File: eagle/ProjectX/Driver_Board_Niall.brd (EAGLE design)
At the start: 100 x 100 mm, 185 parts, among them IC2 NCV78M05BDTRKG, J1 694102303002, U1 TC4427AEOA, U10 TC4427AEOA, U11 TC4427AEOA, U12 TC4427AEOA, U1200 CD74HC4067SM96, U13 TC4427AEOA, U14 TC4427AEOA, U15 TC4427AEOA, U16 TC4427AEOA, U17 TC4427AEOA, U18 TC4427AEOA, U19 TC4427AEOA, U2 TC4427AEOA, U20 TC4427AEOA, U200 ADA4091-2ARZ-RL, U21 TC4427AEOA, U22 TC4427AEOA, U23 TC4427AEOA, U24 TC4427AEOA, U25 TC4427AEOA, U26 TC4427AEOA, U27 TC4427AEOA, U28 TC4427AEOA, U29 TC4427AEOA, U3 TC4427AEOA, U30 TC4427AEOA, U31 TC4427AEOA, U32 TC4427AEOA, U33 TC4427AEOA, U34 TC4427AEOA, U35 TC4427AEOA, U36 TC4427AEOA, U37 TC4427AEOA, U38 TC4427AEOA, U39 TC4427AEOA, U4 TC4427AEOA, U40 TC4427AEOA, U41 TC4427AEOA, U42 TC4427AEOA, U43 TC4427AEOA, U44 TC4427AEOA, U45 TC4427AEOA, U46 TC4427AEOA, U47 TC4427AEOA, U48 TC4427AEOA, U49 TC4427AEOA, U5 TC4427AEOA, U50 TC4427AEOA, U6 TC4427AEOA, U7 TC4427AEOA, U8 TC4427AEOA, U9 TC4427AEOA

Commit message: Niall Boards new layout that should slot together
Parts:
- removed TP1, TP2: TPSTP10SQ, testpad:TP10SQ
- removed TRANSDUCERS_1, TRANSDUCERS_2, TRANSDUCERS_3, TRANSDUCERS_4: 40_PIN_SMD, Parts:40_PIN_SMD
- removed TRANSDUCERS_5: (no value), pinhead:2X20
- added 1, 2, 3, 4: PHB_1MM27_2X25_SNS, _hhn_con_pinhead_box_1mm27:PHB_1MM27_2X25_SNS
- moved LED_8 129.3 mm to (-12.9, 110.2)
- moved LED_9 128.5 mm to (-11.9, 95.4)
- moved LED_7 128.1 mm to (-12.9, 123.1)
- moved LED_10 126.9 mm to (-9.51, 81.2)
- moved 5V-REG 63.9 mm to (2.09, 64.4), turned to 270 degrees
- moved U40 56.3 mm to (72.4, 61.9), turned to 90 degrees
- moved DATA_2 55.1 mm to (-24.1, 61.7)
- moved C40 54.0 mm to (69.0, 61.9), turned to 90 degrees
- moved C12 50.5 mm to (38.5, 54.0), turned to 180 degrees
- moved U38 49.3 mm to (64.2, 61.7), turned to 90 degrees
- moved LED_6 49.0 mm to (-8.36, 72.7)
- moved C38 48.0 mm to (60.7, 61.7), turned to 90 degrees
- moved U12 47.5 mm to (38.5, 50.3), turned to 180 degrees
- moved U20 47.0 mm to (38.5, 7.11), turned to 180 degrees
- moved C29 44.9 mm to (38.5, 46.7), turned to 180 degrees
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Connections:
- removed net N$23: DIP2.8, TP1.TP
- removed net N$24: DIP2.9, TP2.TP
- removed net N$25: DATA_2.9, DIP2.190
- removed net N$26: DATA_2.7, DIP2.193
- removed net N$27: DATA_2.5, DIP2.197
- removed net N$28: DATA_2.1, DIP2.203
- removed net N$29: DATA_2.3, DIP2.200
- net +5V: no longer DATA_1.1
- net 1: now also DIP2.75; no longer DIP2.77
- net 10: now also DIP2.47; no longer DIP2.41
- net 100: now also DIP2.137; no longer DIP2.162
- net 11: now also DIP2.48; no longer DIP2.39
- net 12: now also DIP2.50; no longer DIP2.35
- net 13: now also DIP2.40; no longer DIP2.33
- net 14: now also DIP2.36; no longer DIP2.30
- net 15: now also DIP2.60; no longer DIP2.28
- net 16: now also DIP2.62; no longer DIP2.24
- net 17: now also DIP2.29; no longer DIP2.22
- net 18: now also DIP2.23; no longer DIP2.18
- net 19: now also DIP2.64; no longer DIP2.15
- net 2: now also DIP2.77; no longer DIP2.75
- net 20: now also DIP2.69; no longer DIP2.11
- net 21: now also DIP2.19; no longer DIP2.82
- net 22: now also DIP2.25; no longer DIP2.76
- net 23: now also DIP2.192; no longer DIP2.74
- net 24: now also DIP2.196; no longer DIP2.65
- net 25: now also DIP2.102; no longer DIP2.63
- net 26: now also DIP2.109; no longer DIP2.61
- net 27: now also DIP2.31; no longer DIP2.55
- net 28: now also DIP2.34; no longer DIP2.49
- net 29: now also DIP2.133; no longer DIP2.47
- net 3: now also DIP2.35; no longer DIP2.69
- net 30: now also DIP2.138; no longer DIP2.42
- net 31: now also DIP2.42; no longer DIP2.40
- net 32: now also DIP2.49; no longer DIP2.36
- net 33: now also DIP2.145; no longer DIP2.34
- net 34: now also DIP2.151; no longer DIP2.31
- net 35: now also DIP2.61; no longer DIP2.29
- net 36: now also DIP2.65; no longer DIP2.25
- net 37: now also DIP2.189; no longer DIP2.23
- net 38: now also DIP2.186; no longer DIP2.19
- net 39: now also DIP2.76; no longer DIP2.16
- net 4: now also DIP2.39; no longer DIP2.64
- net 40: now also DIP2.82; no longer DIP2.12
- net 41: now also DIP2.16; no longer DIP2.165
- net 42: now also DIP2.9; no longer DIP2.168
- net 43: now also DIP2.202; no longer DIP2.178
- net 44: now also DIP2.199; no longer DIP2.181
- net 45: now also DIP2.126; no longer DIP2.138
- net 46: now also DIP2.128; no longer DIP2.135
- net 47: now also DIP2.164; no longer DIP2.133
- net 48: now also DIP2.167; no longer DIP2.129
- net 49: now also DIP2.147; no longer DIP2.127
- net 5: now also DIP2.74; no longer DIP2.62
- net 50: now also DIP2.140; no longer DIP2.123
- net 51: now also DIP2.135; no longer DIP2.120
- net 52: now also DIP2.129; no longer DIP2.116
- net 53: now also DIP2.116; no longer DIP2.107
- net 54: now also DIP2.123; no longer DIP2.102
- net 55: now also DIP2.127; no longer DIP2.113
- net 56: now also DIP2.120; no longer DIP2.109
- net 57: now also DIP2.205; no longer DIP2.99
- net 58: now also DIP2.12; no longer DIP2.97
- net 59: now also DIP2.90; no longer DIP2.94
- net 6: now also DIP2.63; no longer DIP2.60
- net 60: now also DIP2.97; no longer DIP2.90
- net 61: now also DIP2.99; no longer DIP2.152
- net 62: now also DIP2.94; no longer DIP2.150
- net 63: now also DIP2.113; no longer DIP2.139
- net 64: now also DIP2.107; no longer DIP2.137
- net 65: now also DIP2.93; no longer DIP2.146
- net 66: now also DIP2.96; no longer DIP2.144
- net 67: now also DIP2.98; no longer DIP2.128
- net 68: now also DIP2.100; no longer DIP2.126
- net 69: now also DIP2.106; no longer DIP2.134
- net 7: now also DIP2.41; no longer DIP2.50
- net 70: now also DIP2.108; no longer DIP2.132
- net 71: now also DIP2.112; no longer DIP2.115
- net 72: now also DIP2.115; no longer DIP2.112
- net 73: now also DIP2.119; no longer DIP2.122
- net 74: now also DIP2.122; no longer DIP2.119
- net 75: now also DIP2.178; no longer DIP2.108
- net 76: now also DIP2.180; no longer DIP2.106
- net 77: now also DIP2.162; no longer DIP2.100
- net 78: now also DIP2.165; no longer DIP2.98
- net 79: now also DIP2.185; no longer DIP2.96
- net 8: now also DIP2.45; no longer DIP2.48
- net 80: now also DIP2.187; no longer DIP2.93
- net 81: now also DIP2.153; no longer DIP2.186
- net 82: now also DIP2.160; no longer DIP2.180
- net 83: now also DIP2.190; no longer DIP2.185
- net 84: now also DIP2.193; no longer DIP2.189
- net 85: now also DIP2.172; no longer DIP2.171
- net 86: now also DIP2.168; no longer DIP2.167
- net 87: now also DIP2.177; no longer DIP2.187
- net 88: now also DIP2.171; no longer DIP2.172
- net 89: now also DIP2.163; no longer DIP2.145
- net 9: now also DIP2.55; no longer DIP2.45
- net 90: now also DIP2.161; no longer DIP2.147
- net 92: now also DIP2.181; no longer DIP2.177
- net 93: now also DIP2.146; no longer DIP2.151
- net 94: now also DIP2.144; no longer DIP2.153
- net 95: now also DIP2.152; no longer DIP2.163
- net 96: now also DIP2.150; no longer DIP2.161
- net 97: now also DIP2.134; no longer DIP2.160
- net 98: now also DIP2.132; no longer DIP2.140
- net 99: now also DIP2.139; no longer DIP2.164
- net FROM_TRANS_100: now also 1.2; no longer TRANSDUCERS_5.1
- net FROM_TRANS_85: now also 1.50; no longer TRANSDUCERS_5.31
- net FROM_TRANS_86: now also 1.48; no longer TRANSDUCERS_5.29
- net FROM_TRANS_87: now also 1.46; no longer TRANSDUCERS_5.27
- net FROM_TRANS_88: now also 1.44; no longer TRANSDUCERS_5.25
- net FROM_TRANS_89: now also 1.42; no longer TRANSDUCERS_5.23
- net FROM_TRANS_90: now also 1.40; no longer TRANSDUCERS_5.21
- net FROM_TRANS_91: now also 1.38; no longer TRANSDUCERS_5.19
- net FROM_TRANS_92: now also 1.36; no longer TRANSDUCERS_5.17
- net FROM_TRANS_93: now also 1.16; no longer TRANSDUCERS_5.15
- net FROM_TRANS_94: now also 1.14; no longer TRANSDUCERS_5.13
- net FROM_TRANS_95: now also 1.12; no longer TRANSDUCERS_5.11
- net FROM_TRANS_96: now also 1.10; no longer TRANSDUCERS_5.9
- net FROM_TRANS_97: now also 1.8; no longer TRANSDUCERS_5.7
- net FROM_TRANS_98: now also 1.6; no longer TRANSDUCERS_5.5
- net FROM_TRANS_99: now also 1.4; no longer TRANSDUCERS_5.3
- net GND: now also 1.18, 1.20, 1.22, 1.24, 1.26, 1.28, 1.30, 1.32, 1.34, 2.10, 2.11, 2.14, 2.15, 2.18, 2.19, 2.2, 2.22, 2.23, 2.26, 2.27, 2.3, 2.30, 2.31, 2.34, 2.35, 2.38, 2.39, 2.42, 2.43, 2.46, 2.47, 2.50, 2.6, 2.7, 3.10, 3.11, 3.14, 3.15, 3.18, 3.19, 3.2, 3.22, 3.23, 3.26, 3.27, 3.3, 3.30, 3.31, 3.34, 3.35, 3.38, 3.39, 3.42, 3.43, 3.46, 3.47, 3.50, 3.6, 3.7, 4.10, 4.11, 4.14, 4.15, 4.18, 4.19, 4.2, 4.22, 4.23, 4.26, 4.27, 4.3, 4.30, 4.31, 4.34, 4.35, 4.38, 4.39, 4.42, 4.43, 4.46, 4.47, 4.50, 4.6, 4.7; no longer DATA_1.2, DATA_2.2, TRANSDUCERS_1.1, TRANSDUCERS_1.11, TRANSDUCERS_1.13, TRANSDUCERS_1.15, TRANSDUCERS_1.17, TRANSDUCERS_1.19, TRANSDUCERS_1.21, TRANSDUCERS_1.23, TRANSDUCERS_1.25, TRANSDUCERS_1.27, TRANSDUCERS_1.29, TRANSDUCERS_1.3, TRANSDUCERS_1.31, TRANSDUCERS_1.33, TRANSDUCERS_1.35, TRANSDUCERS_1.37, TRANSDUCERS_1.39, TRANSDUCERS_1.5, TRANSDUCERS_1.7, TRANSDUCERS_1.9, TRANSDUCERS_2.1, TRANSDUCERS_2.11, TRANSDUCERS_2.13, TRANSDUCERS_2.15, TRANSDUCERS_2.17, TRANSDUCERS_2.19, TRANSDUCERS_2.21, TRANSDUCERS_2.23, TRANSDUCERS_2.25, TRANSDUCERS_2.27, TRANSDUCERS_2.29, TRANSDUCERS_2.3, TRANSDUCERS_2.31, TRANSDUCERS_2.33, TRANSDUCERS_2.35, TRANSDUCERS_2.37, TRANSDUCERS_2.39, TRANSDUCERS_2.5, TRANSDUCERS_2.7, TRANSDUCERS_2.9, TRANSDUCERS_3.1, TRANSDUCERS_3.11, TRANSDUCERS_3.13, TRANSDUCERS_3.15, TRANSDUCERS_3.17, TRANSDUCERS_3.19, TRANSDUCERS_3.21, TRANSDUCERS_3.23, TRANSDUCERS_3.25, TRANSDUCERS_3.27, TRANSDUCERS_3.29, TRANSDUCERS_3.3, TRANSDUCERS_3.31, TRANSDUCERS_3.33, TRANSDUCERS_3.35, TRANSDUCERS_3.37, TRANSDUCERS_3.39, TRANSDUCERS_3.5, TRANSDUCERS_3.7, TRANSDUCERS_3.9, TRANSDUCERS_4.1, TRANSDUCERS_4.11, TRANSDUCERS_4.13, TRANSDUCERS_4.15, TRANSDUCERS_4.17, TRANSDUCERS_4.19, TRANSDUCERS_4.21, TRANSDUCERS_4.23, TRANSDUCERS_4.25, TRANSDUCERS_4.27, TRANSDUCERS_4.29, TRANSDUCERS_4.3, TRANSDUCERS_4.31, TRANSDUCERS_4.33, TRANSDUCERS_4.35, TRANSDUCERS_4.37, TRANSDUCERS_4.39, TRANSDUCERS_4.5, TRANSDUCERS_4.7, TRANSDUCERS_4.9, TRANSDUCERS_5.33, TRANSDUCERS_5.35, TRANSDUCERS_5.37, TRANSDUCERS_5.39
- net TEENSY_DATA_0: no longer DATA_1.7
- net TEENSY_DATA_1: no longer DATA_1.9
- net TEENSY_DATA_10: no longer DATA_2.10
- net TEENSY_DATA_11: no longer DATA_1.5
- net TEENSY_DATA_12: no longer DATA_1.3
- net TEENSY_DATA_2: no longer DATA_1.4
- net TEENSY_DATA_3: no longer DATA_1.6
- net TEENSY_DATA_31: no longer DIP2.3
- net TEENSY_DATA_32: no longer DIP2.5
- net TEENSY_DATA_33: no longer DIP2.2
- net TEENSY_DATA_34: no longer DIP2.4
- net TEENSY_DATA_4: no longer DATA_1.8
- net TEENSY_DATA_5: no longer DATA_1.10
- net TEENSY_DATA_7: no longer DATA_2.4
- net TEENSY_DATA_8: no longer DATA_2.6
- net TEENSY_DATA_9: no longer DATA_2.8
- net TO_TRAN_1: now also 4.9; no longer TRANSDUCERS_1.2
- net TO_TRAN_10: now also 4.16; no longer TRANSDUCERS_1.20
- net TO_TRAN_100: now also 1.1; no longer TRANSDUCERS_5.2
- net TO_TRAN_11: now also 4.33; no longer TRANSDUCERS_1.22
- net TO_TRAN_12: now also 4.29; no longer TRANSDUCERS_1.24
- net TO_TRAN_13: now also 4.20; no longer TRANSDUCERS_1.26
- net TO_TRAN_14: now also 4.24; no longer TRANSDUCERS_1.28
- net TO_TRAN_15: now also 4.25; no longer TRANSDUCERS_1.30
- net TO_TRAN_16: now also 4.21; no longer TRANSDUCERS_1.32
- net TO_TRAN_17: now also 4.28; no longer TRANSDUCERS_1.34
- net TO_TRAN_18: now also 4.32; no longer TRANSDUCERS_1.36
- net TO_TRAN_19: now also 4.17; no longer TRANSDUCERS_1.38
- net TO_TRAN_2: now also 4.5; no longer TRANSDUCERS_1.4
- net TO_TRAN_20: now also 4.13; no longer TRANSDUCERS_1.40
- net TO_TRAN_21: now also 3.33; no longer TRANSDUCERS_2.2
- net TO_TRAN_22: now also 3.29; no longer TRANSDUCERS_2.4
- net TO_TRAN_23: now also 3.49; no longer TRANSDUCERS_2.6
- net TO_TRAN_24: now also 3.45; no longer TRANSDUCERS_2.8
- net TO_TRAN_25: now also 3.12; no longer TRANSDUCERS_2.10
- net TO_TRAN_26: now also 3.16; no longer TRANSDUCERS_2.12
- net TO_TRAN_27: now also 3.25; no longer TRANSDUCERS_2.14
- net TO_TRAN_28: now also 3.21; no longer TRANSDUCERS_2.16
- net TO_TRAN_29: now also 3.28; no longer TRANSDUCERS_2.18
- net TO_TRAN_3: now also 4.49; no longer TRANSDUCERS_1.6
- net TO_TRAN_30: now also 3.32; no longer TRANSDUCERS_2.20
- net TO_TRAN_31: now also 3.17; no longer TRANSDUCERS_2.22
- net TO_TRAN_32: now also 3.13; no longer TRANSDUCERS_2.24
- net TO_TRAN_33: now also 3.36; no longer TRANSDUCERS_2.26
- net TO_TRAN_34: now also 3.40; no longer TRANSDUCERS_2.28
- net TO_TRAN_35: now also 3.9; no longer TRANSDUCERS_2.30
- net TO_TRAN_36: now also 3.5; no longer TRANSDUCERS_2.32
- net TO_TRAN_37: now also 3.44; no longer TRANSDUCERS_2.34
- net TO_TRAN_38: now also 3.48; no longer TRANSDUCERS_2.36
- net TO_TRAN_39: now also 3.1; no longer TRANSDUCERS_2.38
- net TO_TRAN_4: now also 4.45; no longer TRANSDUCERS_1.8
- net TO_TRAN_40: now also 4.1; no longer TRANSDUCERS_2.40
- net TO_TRAN_41: now also 4.36; no longer TRANSDUCERS_3.2
- net TO_TRAN_42: now also 4.40; no longer TRANSDUCERS_3.4
- net TO_TRAN_43: now also 4.44; no longer TRANSDUCERS_3.6
- net TO_TRAN_44: now also 4.48; no longer TRANSDUCERS_3.8
- net TO_TRAN_45: now also 2.44; no longer TRANSDUCERS_3.10
- net TO_TRAN_46: now also 2.48; no longer TRANSDUCERS_3.12
- net TO_TRAN_47: now also 2.45; no longer TRANSDUCERS_3.14
- net TO_TRAN_48: now also 2.41; no longer TRANSDUCERS_3.16
- net TO_TRAN_49: now also 2.37; no longer TRANSDUCERS_3.18
- net TO_TRAN_5: now also 4.4; no longer TRANSDUCERS_1.10
- net TO_TRAN_50: now also 2.33; no longer TRANSDUCERS_3.20
- net TO_TRAN_51: now also 2.29; no longer TRANSDUCERS_3.22
- net TO_TRAN_52: now also 2.25; no longer TRANSDUCERS_3.24
- net TO_TRAN_53: now also 3.20; no longer TRANSDUCERS_3.26
- net TO_TRAN_54: now also 3.24; no longer TRANSDUCERS_3.28
- net TO_TRAN_55: now also 2.21; no longer TRANSDUCERS_3.30
- net TO_TRAN_56: now also 2.17; no longer TRANSDUCERS_3.32
- net TO_TRAN_57: now also 3.41; no longer TRANSDUCERS_3.34
- net TO_TRAN_58: now also 3.37; no longer TRANSDUCERS_3.36
- net TO_TRAN_59: now also 3.4; no longer TRANSDUCERS_3.38
- net TO_TRAN_6: now also 4.8; no longer TRANSDUCERS_1.12
- net TO_TRAN_60: now also 3.8; no longer TRANSDUCERS_3.40
- net TO_TRAN_61: now also 2.5; no longer TRANSDUCERS_4.2
- net TO_TRAN_62: now also 2.1; no longer TRANSDUCERS_4.4
- net TO_TRAN_63: now also 2.13; no longer TRANSDUCERS_4.6
- net TO_TRAN_64: now also 2.9; no longer TRANSDUCERS_4.8
- net TO_TRAN_65: now also 2.4; no longer TRANSDUCERS_4.10
- net TO_TRAN_66: now also 2.8; no longer TRANSDUCERS_4.12
- net TO_TRAN_67: now also 2.12; no longer TRANSDUCERS_4.14
- net TO_TRAN_68: now also 2.16; no longer TRANSDUCERS_4.16
- net TO_TRAN_69: now also 2.20; no longer TRANSDUCERS_4.18
- net TO_TRAN_7: now also 4.41; no longer TRANSDUCERS_1.14
- net TO_TRAN_70: now also 2.24; no longer TRANSDUCERS_4.20
- net TO_TRAN_71: now also 2.28; no longer TRANSDUCERS_4.22
- net TO_TRAN_72: now also 2.32; no longer TRANSDUCERS_4.24
- net TO_TRAN_73: now also 2.36; no longer TRANSDUCERS_4.26
- net TO_TRAN_74: now also 2.40; no longer TRANSDUCERS_4.28
- net TO_TRAN_75: now also 2.49; no longer TRANSDUCERS_4.30
- net TO_TRAN_76: now also 1.33; no longer TRANSDUCERS_4.32
- net TO_TRAN_77: now also 1.31; no longer TRANSDUCERS_4.34
- net TO_TRAN_78: now also 1.29; no longer TRANSDUCERS_4.36
- net TO_TRAN_79: now also 1.27; no longer TRANSDUCERS_4.38
- net TO_TRAN_8: now also 4.37; no longer TRANSDUCERS_1.16
- net TO_TRAN_80: now also 1.25; no longer TRANSDUCERS_4.40
- net TO_TRAN_81: now also 1.23; no longer TRANSDUCERS_5.40
- net TO_TRAN_82: now also 1.21; no longer TRANSDUCERS_5.38
- net TO_TRAN_83: now also 1.19; no longer TRANSDUCERS_5.36
- net TO_TRAN_84: now also 1.17; no longer TRANSDUCERS_5.34
- net TO_TRAN_85: now also 1.49; no longer TRANSDUCERS_5.32
- net TO_TRAN_86: now also 1.47; no longer TRANSDUCERS_5.30
- net TO_TRAN_87: now also 1.45; no longer TRANSDUCERS_5.28
- net TO_TRAN_88: now also 1.43; no longer TRANSDUCERS_5.26
- net TO_TRAN_89: now also 1.41; no longer TRANSDUCERS_5.24
- net TO_TRAN_9: now also 4.12; no longer TRANSDUCERS_1.18
- net TO_TRAN_90: now also 1.39; no longer TRANSDUCERS_5.22
- net TO_TRAN_91: now also 1.37; no longer TRANSDUCERS_5.20
- net TO_TRAN_92: now also 1.35; no longer TRANSDUCERS_5.18
- net TO_TRAN_93: now also 1.15; no longer TRANSDUCERS_5.16
- net TO_TRAN_94: now also 1.13; no longer TRANSDUCERS_5.14
- net TO_TRAN_95: now also 1.11; no longer TRANSDUCERS_5.12
- net TO_TRAN_96: now also 1.9; no longer TRANSDUCERS_5.10
- net TO_TRAN_97: now also 1.7; no longer TRANSDUCERS_5.8
- net TO_TRAN_98: now also 1.5; no longer TRANSDUCERS_5.6
- net TO_TRAN_99: now also 1.3; no longer TRANSDUCERS_5.4
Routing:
- net +5V: track 361.9 -> 205.0 mm, vias 7 -> 2
- net GND: track 499.3 -> 351.7 mm, vias 170 -> 163
- net N$22: track 103.0 -> 0.00 mm, vias 2 -> 0
- net N$18: track 76.9 -> 0.00 mm
- net TEENSY_DATA_33: track 59.0 -> 0.00 mm, vias 4 -> 0
- net TEENSY_DATA_34: track 56.2 -> 0.00 mm
- net TEENSY_DATA_32: track 50.2 -> 0.00 mm, vias 2 -> 0
- net TEENSY_DATA_12: track 46.1 -> 0.00 mm, vias 2 -> 0
- net TEENSY_DATA_31: track 44.2 -> 0.00 mm, vias 2 -> 0
- net TEENSY_DATA_1: track 40.0 -> 0.00 mm, vias 1 -> 0
- net TO_TRAN_75: track 3.37 -> 42.4 mm
- net TEENSY_DATA_11: track 38.7 -> 0.00 mm, vias 2 -> 0
- net 80: track 8.90 -> 44.3 mm
- net N$16: track 33.9 -> 0.00 mm
- net TEENSY_DATA_0: track 33.7 -> 0.00 mm, vias 1 -> 0
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
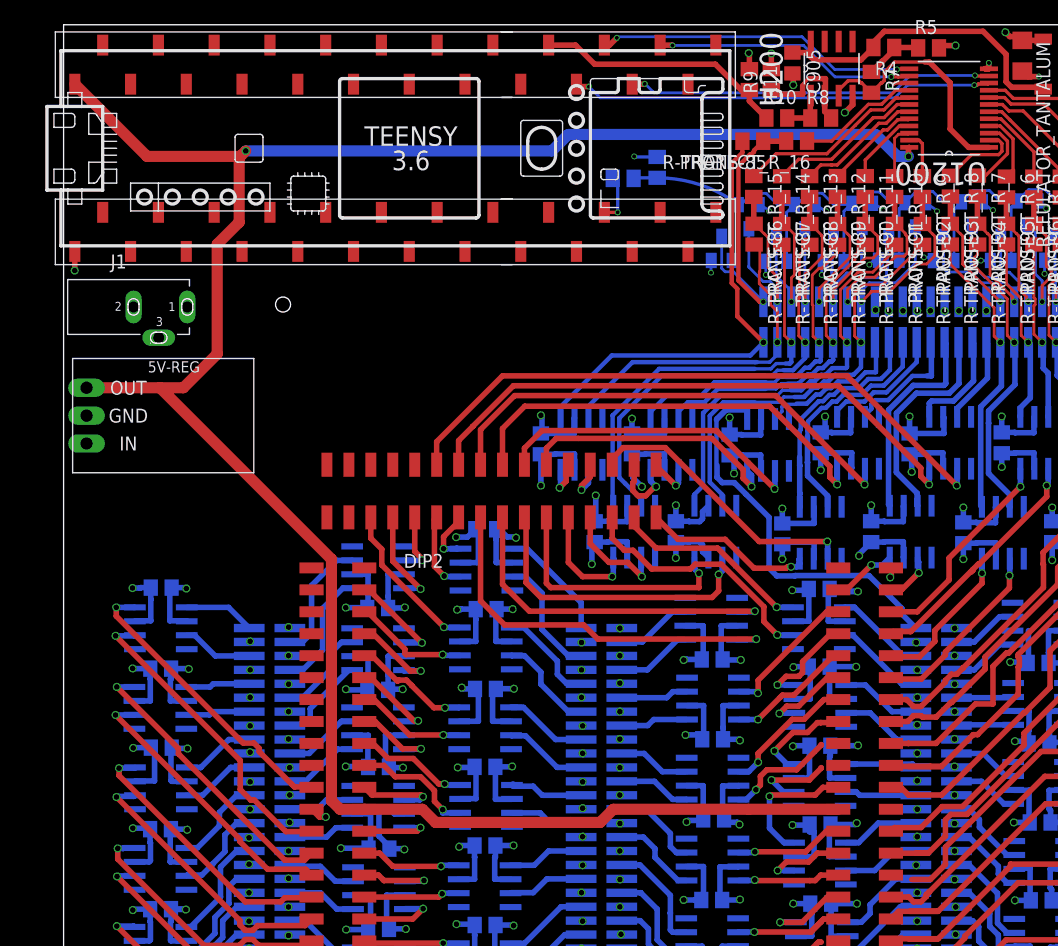
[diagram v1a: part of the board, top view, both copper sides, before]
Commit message: Added capasitors to inputs
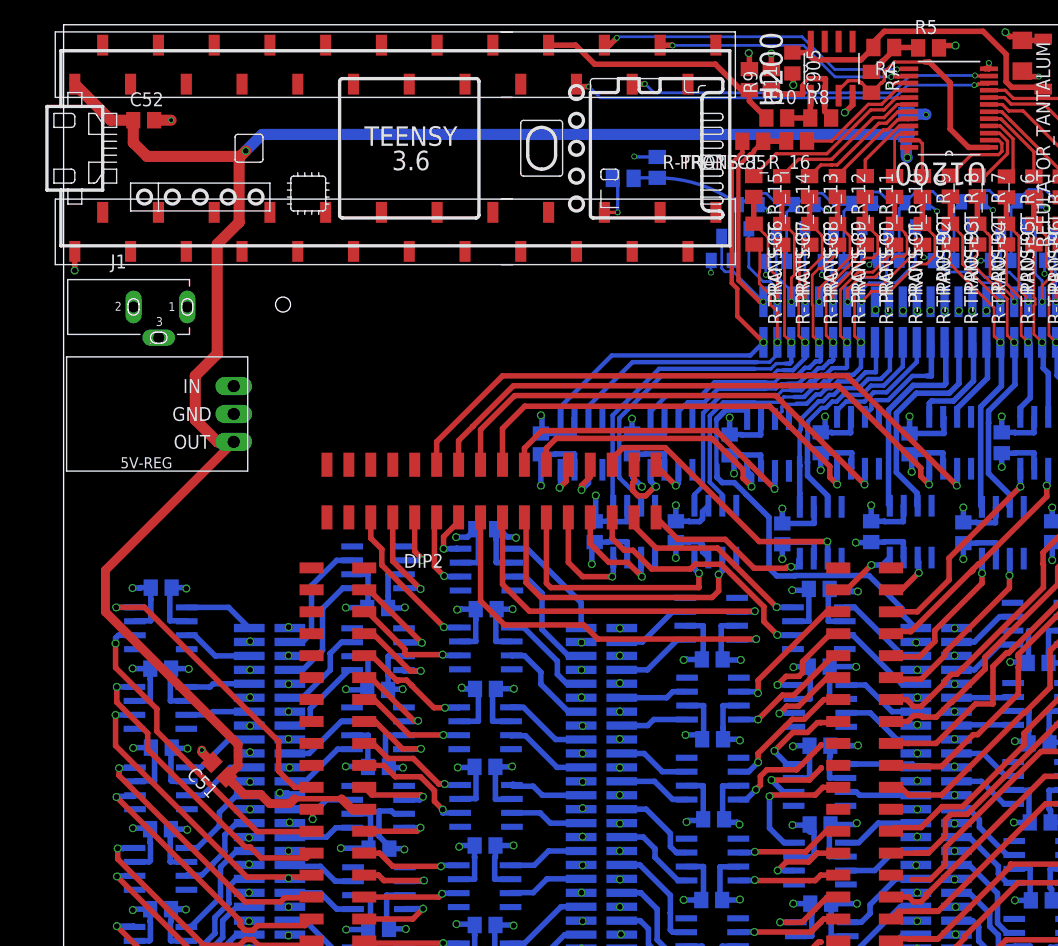
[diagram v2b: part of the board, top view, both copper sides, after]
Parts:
- added C51, C52, C53: 100nF, resistor:C0805
- moved 5V-REG 13.4 mm to (15.5, 64.5), turned to 90 degrees
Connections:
- net +5V: now also C51.1, C52.1, C53.1; no longer DIP2.5V@1
- net GND: now also C51.2, C52.2, C53.2; no longer DIP2.GND@1, DIP2.GND@2, DIP2.GND@3
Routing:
- net +5V: track 205.0 -> 170.5 mm
- net GND: track 351.7 -> 355.4 mm, vias 163 -> 165
- net 8: track 25.7 -> 27.4 mm
- net 7: track 26.4 -> 27.7 mm
- net 4: track 28.6 -> 29.8 mm
- net 3: track 27.0 -> 28.0 mm

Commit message: Niall board more work
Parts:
- moved J1 0.41 mm to (0.27, 73.9)
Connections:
- net 3: now also DIP2.8; no longer DIP2.35
- net GND: now also DIP2.GND@2; no longer DIP2.GND@4
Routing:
- net +5V: track 170.5 -> 162.8 mm
- net 3: track 28.0 -> 22.8 mm
- net 8: track 27.4 -> 28.0 mm

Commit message: More cleaning
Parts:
- added C54: 100nF, resistor:C0805
- added UA78M05CDCY: (no value), linear-technology:SOT223
- C53: value 100nF -> 330nF
- moved C51 11.4 mm to (24.3, 26.8), flipped to the bottom, turned to 0 degrees
- moved C53 4.33 mm to (80.1, 88.1), turned to 270 degrees
- moved C7 1.20 mm to (29.9, 24.9)
- moved U7 1.20 mm to (29.9, 28.7)
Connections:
- new net N$23: C54.2, U1200.24, UA78M05CDCY.3
- net +5V: no longer C53.1, U1200.24
- net GND: now also C53.1, C54.1, DIP2.GND@4, UA78M05CDCY.2, UA78M05CDCY.4; no longer C53.2, DIP2.GND@2
- net VDD: now also C53.2, UA78M05CDCY.1
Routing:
- net +5V: track 162.8 -> 84.6 mm, vias 2 -> 1
- net N$23: track 0.00 -> 12.7 mm, vias 0 -> 1
- net GND: track 355.5 -> 364.7 mm, vias 165 -> 164
- net VDD: track 320.2 -> 323.6 mm, vias 51 -> 52
- net 98: track 32.9 -> 29.9 mm
- net 70: track 25.5 -> 22.8 mm
- net 71: track 25.9 -> 23.3 mm
- net TO_TRAN_13: track 6.04 -> 8.49 mm
- net 14: track 7.53 -> 5.30 mm
- net 26: track 11.0 -> 9.63 mm
- net TO_TRAN_75: track 42.4 -> 41.1 mm
- net TO_TRAN_14: track 6.04 -> 7.24 mm
- net 13: track 6.76 -> 7.96 mm
- net N$78: track 4.29 -> 5.44 mm
- net 67: track 22.3 -> 21.3 mm
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
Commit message: More DRC fixes
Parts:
- moved C905 0.51 mm to (66.5, 97.0)
- moved C51 0.32 mm to (24.4, 27.1)
- moved R11 0.10 mm to (62.4, 95.0)
- moved R-TRANS-85 0.10 mm to (62.7, 89.4)
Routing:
- net N$14: track 10.1 -> 9.50 mm

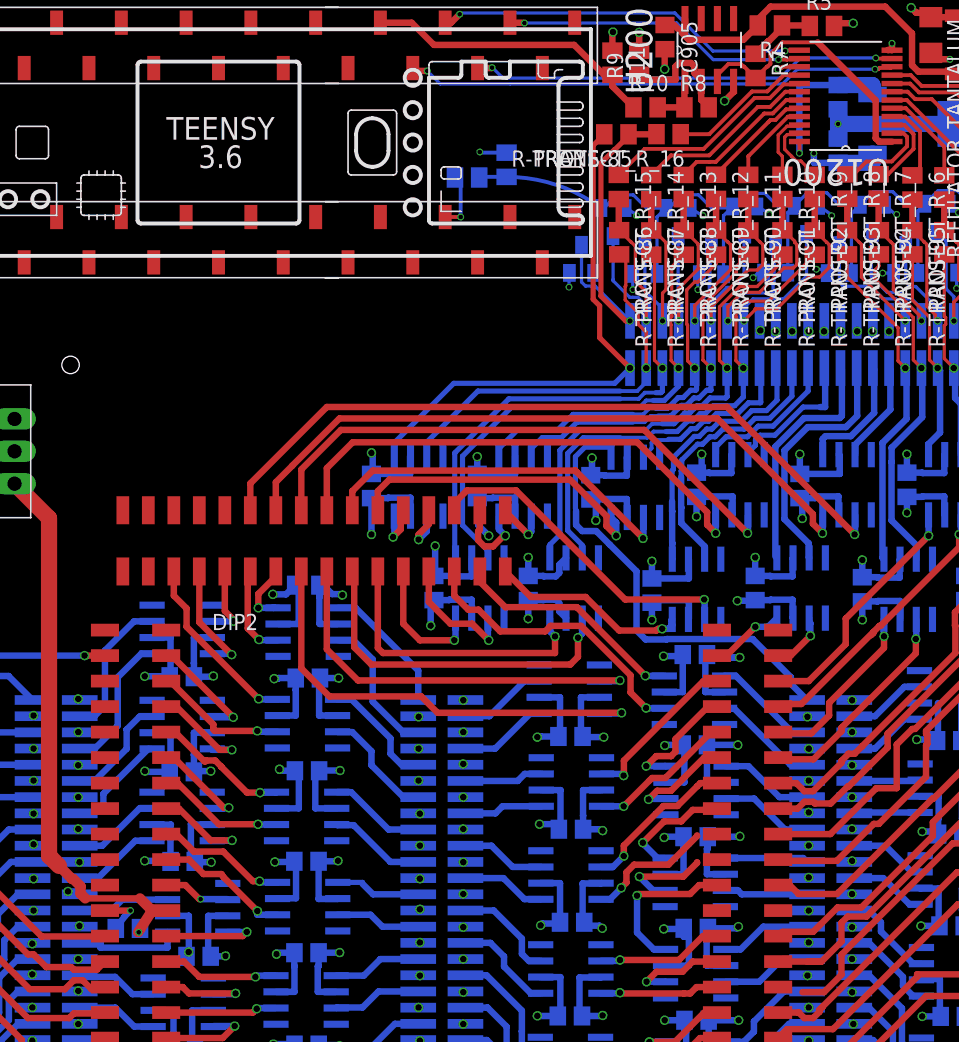
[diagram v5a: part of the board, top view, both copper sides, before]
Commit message: More DRC fixes, just about all done
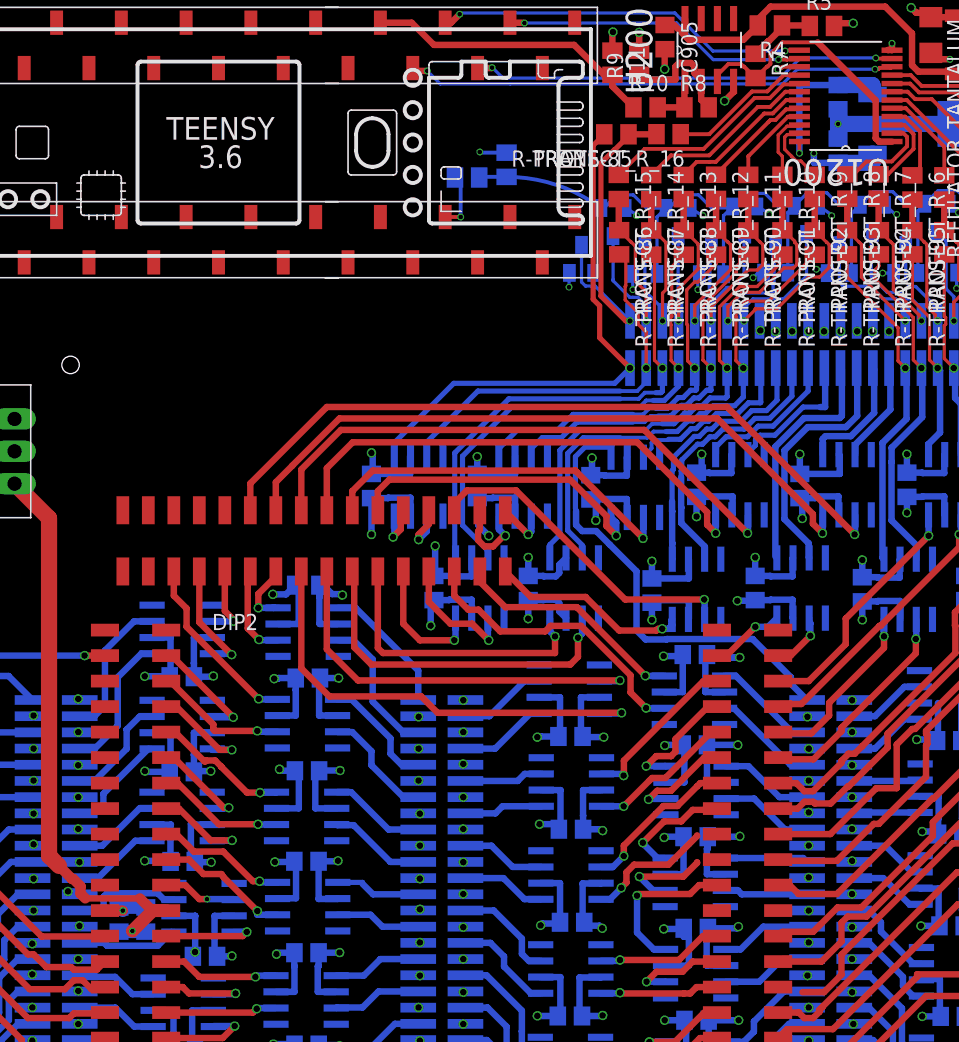
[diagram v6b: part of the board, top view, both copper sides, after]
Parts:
- added C55: 100nF, resistor:C0805
- moved C51 0.99 mm to (23.7, 27.8), turned to 90 degrees
- moved C7 0.50 mm to (30.4, 24.9)
- moved U7 0.50 mm to (30.4, 28.7)
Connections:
- net +5V: now also C55.1
- net GND: now also C55.2
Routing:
- net +5V: track 84.6 -> 87.9 mm
- net TO_TRAN_14: track 7.24 -> 8.79 mm
- net TO_TRAN_48: track 8.94 -> 7.57 mm
- net 74: track 27.2 -> 26.1 mm
- net TO_TRAN_51: track 7.53 -> 6.54 mm
- net TO_TRAN_13: track 8.49 -> 7.93 mm
- net 13: track 7.96 -> 7.46 mm

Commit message: Tweak
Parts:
- moved C52 5.33 mm to (2.00, 91.9)
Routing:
- net GND: track 365.3 -> 363.7 mm
- net +5V: track 87.9 -> 88.7 mm

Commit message: Bit more work
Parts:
- added C56: 100nF, resistor:C0805
- added J2: 694102303002, SnapEDA-Library:69410X303002
- added JP1: JUMPER-SMT_2_NC_TRACE_SILK, SparkFun-Jumpers:SMT-JUMPER_2_NC_TRACE_SILK
- added JP3: JUMPER-SMT_2_NO_SILK, SparkFun-Jumpers:SMT-JUMPER_2_NO_SILK
- moved DATA_1 34.5 mm to (6.86, 53.8)
- moved DATA_2 31.1 mm to (6.86, 59.4)
- moved 5V-REG 5.18 mm to (15.0, 69.7), turned to 270 degrees
- moved C52 3.28 mm to (2.70, 88.7), turned to 270 degrees
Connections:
- new net N$24: 5V-REG.IN, J2.1, JP1.1
- new net N$25: C52.1, C56.1, JP3.1, U$1.VIN3
- net +5V: now also JP3.2; no longer C52.1, U$1.VIN3
- net GND: now also C56.2, J2.2
- net VDD: now also JP1.2; no longer 5V-REG.IN
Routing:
- net GND: track 363.7 -> 377.6 mm, vias 164 -> 163
- net N$25: track 0.00 -> 9.44 mm
- net +5V: track 88.7 -> 81.3 mm, vias 1 -> 3
- net N$24: track 0.00 -> 5.78 mm
- net VDD: track 323.6 -> 325.6 mm, vias 52 -> 53
